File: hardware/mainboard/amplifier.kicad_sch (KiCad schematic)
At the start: 66 parts

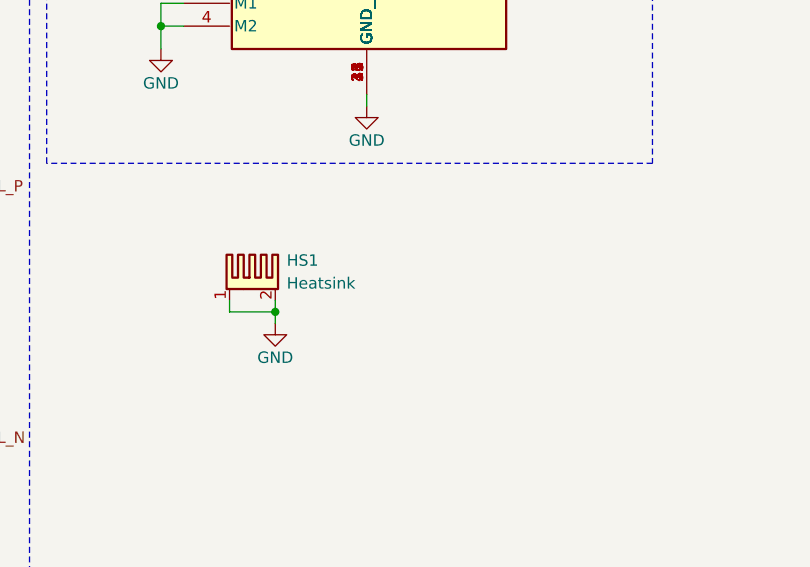
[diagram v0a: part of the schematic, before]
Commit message: Add power supply and front panel PCBs
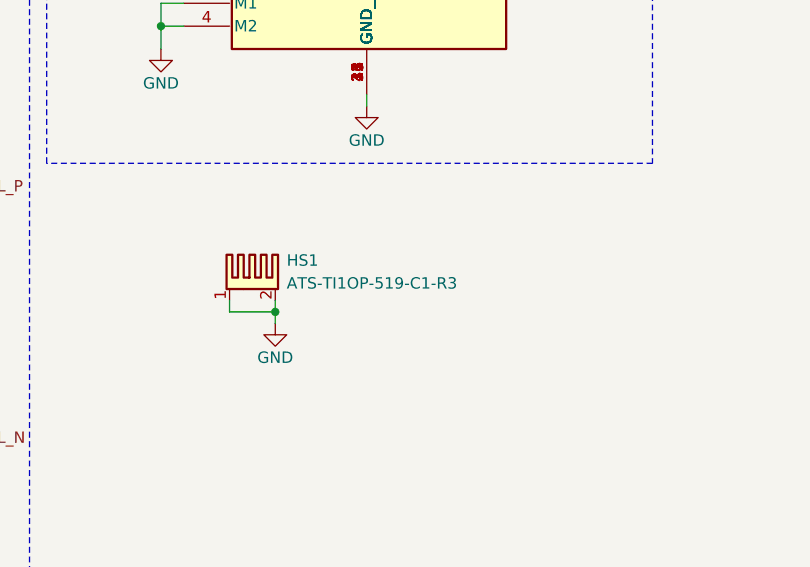
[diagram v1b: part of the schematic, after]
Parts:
- HS1: value Heatsink -> ATS-TI1OP-519-C1-R3
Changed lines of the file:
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@@
 			)
 		)
-		(property "Value" "Heatsink"
+		(property "Value" "ATS-TI1OP-519-C1-R3"
 			(at 148.59 117.4749 0)
 			(show_name no)

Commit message: Prepare PCB for production
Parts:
- C114, C115, C118, C121, C28, C65, C72, C73: Manufacturer_Part_Number (none) -> CC1206JRNPOBBN221
- C116, C119, C70, C71: Manufacturer_Part_Number (none) -> CL21B105KAFNNNE
- C124, C125, C66, C67: Manufacturer_Part_Number (none) -> CL21B224KBFNNNG
- C74, C75, C76, C77: Manufacturer_Part_Number (none) -> 1206B333K101CT
- C78, C80, C85, C86, C89, C90, C91: Manufacturer_Part_Number (none) -> CL10A105KB8NNNC
- C79: Manufacturer_Part_Number (none) -> CC0603KRX7R9BB473
- C81, C82, C83: Manufacturer_Part_Number (none) -> 0603B104K500CT
- C84: Manufacturer_Part_Number (none) -> TAJC107K016RNJ
- C87, C88: Manufacturer_Part_Number (none) -> EWH1JM102L25OT
- HS1: Manufacturer_Part_Number (none) -> ATS-TI1OP-519-C1-R3
- R19, R20, R77, R78: Manufacturer_Part_Number (none) -> RC0805FR-071RL
- R42, R43: Manufacturer_Part_Number (none) -> AC0603FR-073R3L
- R44: Manufacturer_Part_Number (none) -> ERJPA3F3002V
- R45: Manufacturer_Part_Number (none) -> WR06X2202FTL
- R59, R60, R73, R75: Manufacturer_Part_Number (none) -> RC0805FR-0710KL
- R61, R62, R74, R76: Manufacturer_Part_Number (none) -> RC0805FR-0733KL
- R63, R68, R83, R84: Manufacturer_Part_Number (none) -> WR06X2701FTL
